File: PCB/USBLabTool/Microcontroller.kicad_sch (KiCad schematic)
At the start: 14 parts, among them U12 STM32H562VGTx, Y1 32.768kHz

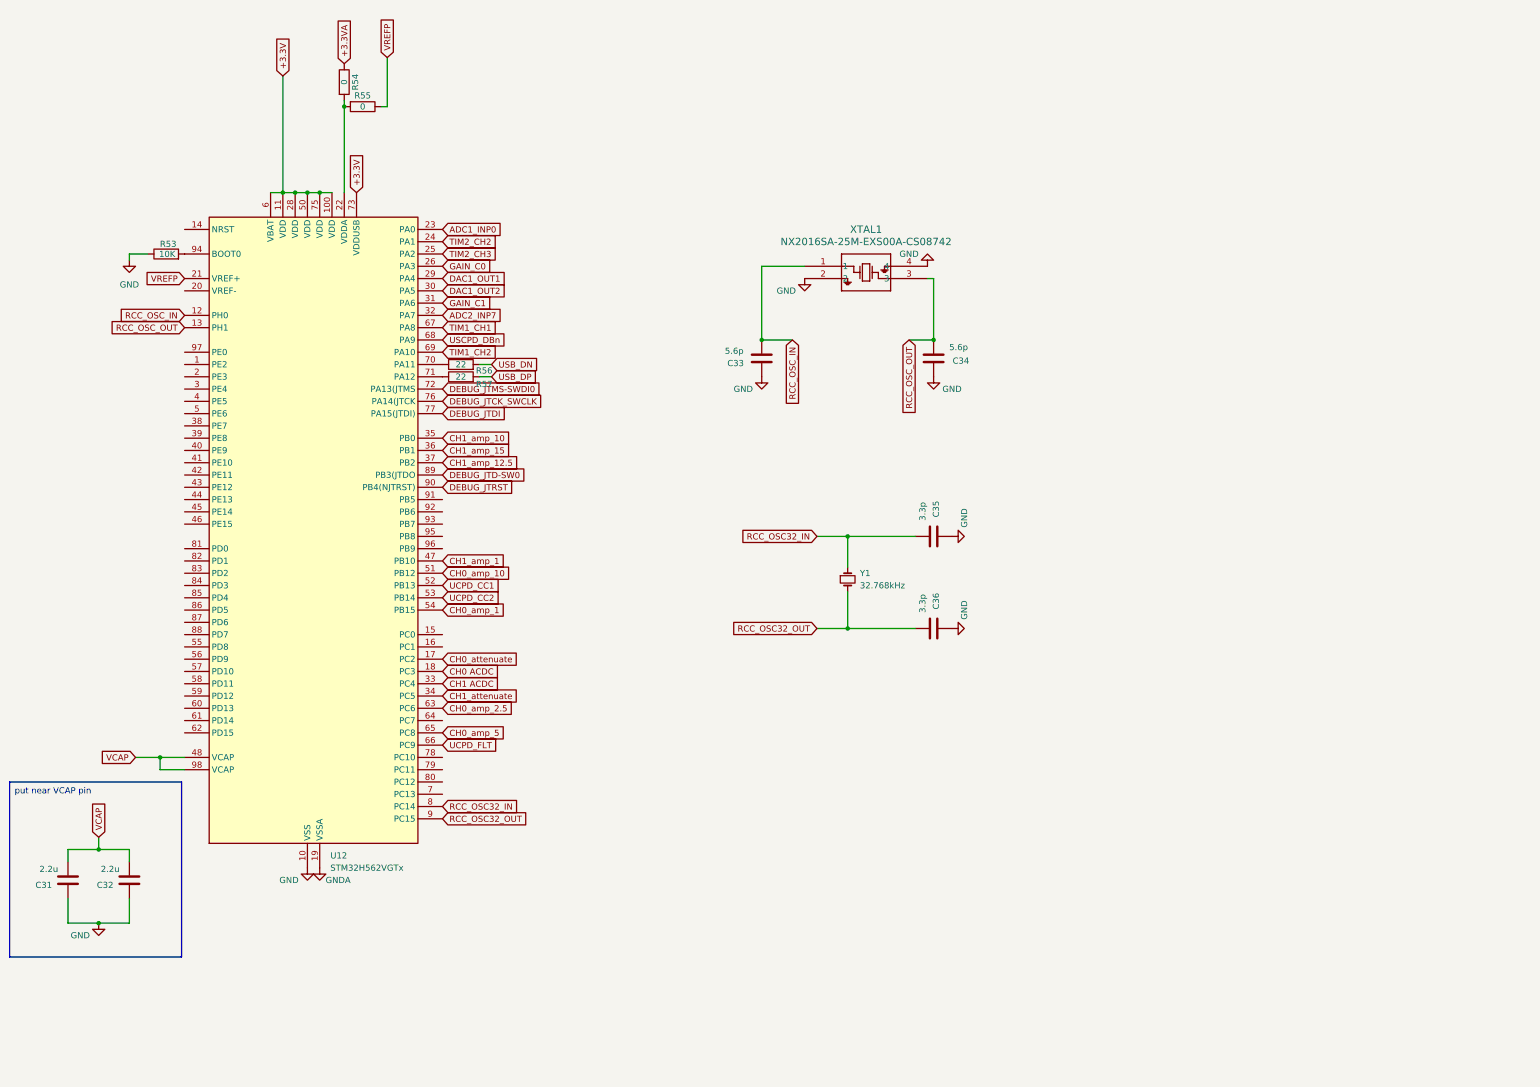
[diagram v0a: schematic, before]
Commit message: add NRST button and change MCU pins as latest
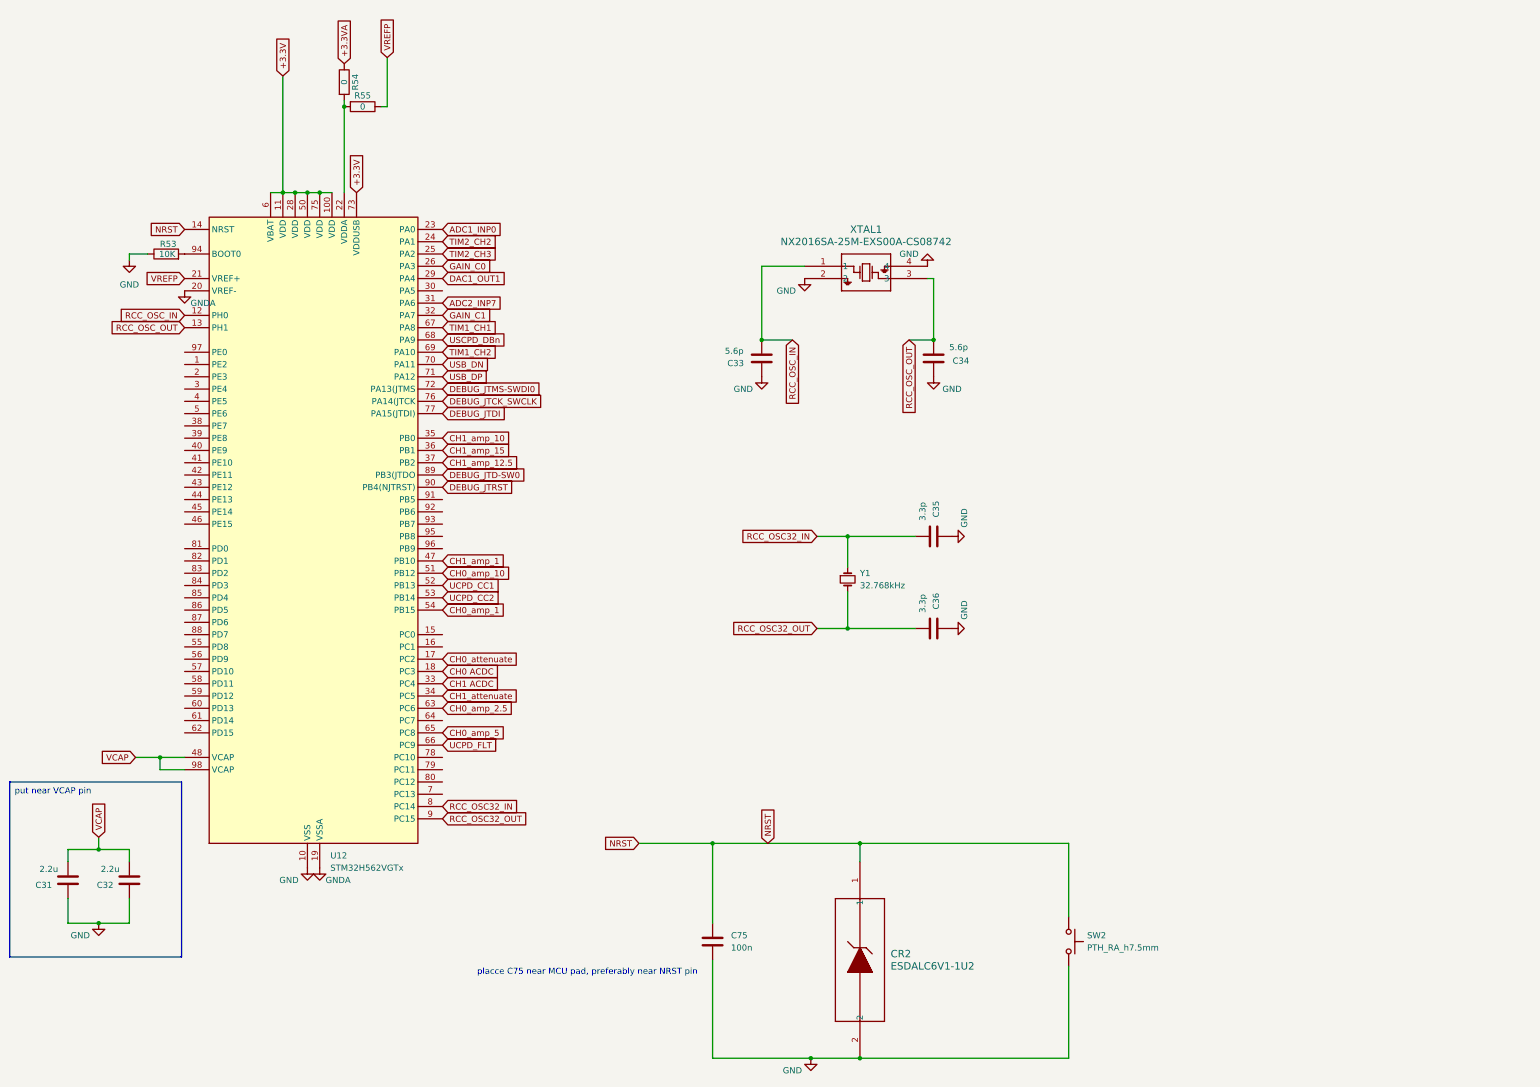
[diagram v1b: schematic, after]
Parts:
- removed R56, R57: 22, Resistor_SMD:R_0603_1608Metric_Pad0.98x0.95mm_HandSolder, symbol Device:R
- added C75: 100n, Capacitor_SMD:C_0603_1608Metric_Pad1.08x0.95mm_HandSolder, symbol Device:C
- added CR2: ESDALC6V1-1U2, DIODE_ESDALC6V1-1U2_STM, symbol ESDALC6V1-1U2:ESDALC6V1-1U2
- added SW2: PTH_RA_h7.5mm, SparkFun-Switch:Push_PTH_RA_8-020_h7.5mm, symbol SparkFun-Switch:SPST_Push_PTH_RA_h7.5mm
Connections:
- net ADC2_INP7: now also U12.31 (PA6); no longer U12.32 (PA7)
- net GAIN_C1: now also U12.32 (PA7); no longer U12.31 (PA6)
- net GND: now also C75.2, CR2.2, SW2.2
- net GNDA: now also U12.20 (VREF-)
- net USB_DN: now also U12.70 (PA11)
- net USB_DP: now also U12.71 (PA12)
- net NRST: now reaches U12.14 (NRST)
- net NRST: now also C75.1, CR2.1, SW2.1
- net DAC1_OUT2: no longer names the net of U12.30 (PA5)
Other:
- note added: "placce C75 near MCU pad, preferably near NRST pin"

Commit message: Fixed up footprints
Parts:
- SW2: footprint SparkFun-Switch:Push_PTH_RA_8-020_h7.5mm -> Button_Switch_THT:SW_PUSH_6mm_H7.3mm
- XTAL1: footprint footprintsgit:NX2016SA_NDK -> userfp:NX2016SA_NDK
- Y1: footprint SparkFun-Clock:Crystal_SMD_3.2x1.5mm -> Crystal:Crystal_SMD_MicroCrystal_CC7V-T1A-2Pin_3.2x1.5mm_HandSoldering

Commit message: Started adding 20pin
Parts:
- added J21: Conn_01x20_Pin, Connector_PinHeader_2.54mm:PinHeader_1x20_P2.54mm_Vertical, symbol Connector:Conn_01x20_Pin
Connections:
- net GND: now also J21.18 (Pin_18)
- net GNDA: now also J21.17 (Pin_17)
- new net P_CH0_IN: J21.20 (Pin_20)
- new net P_CH1_IN: J21.19 (Pin_19)

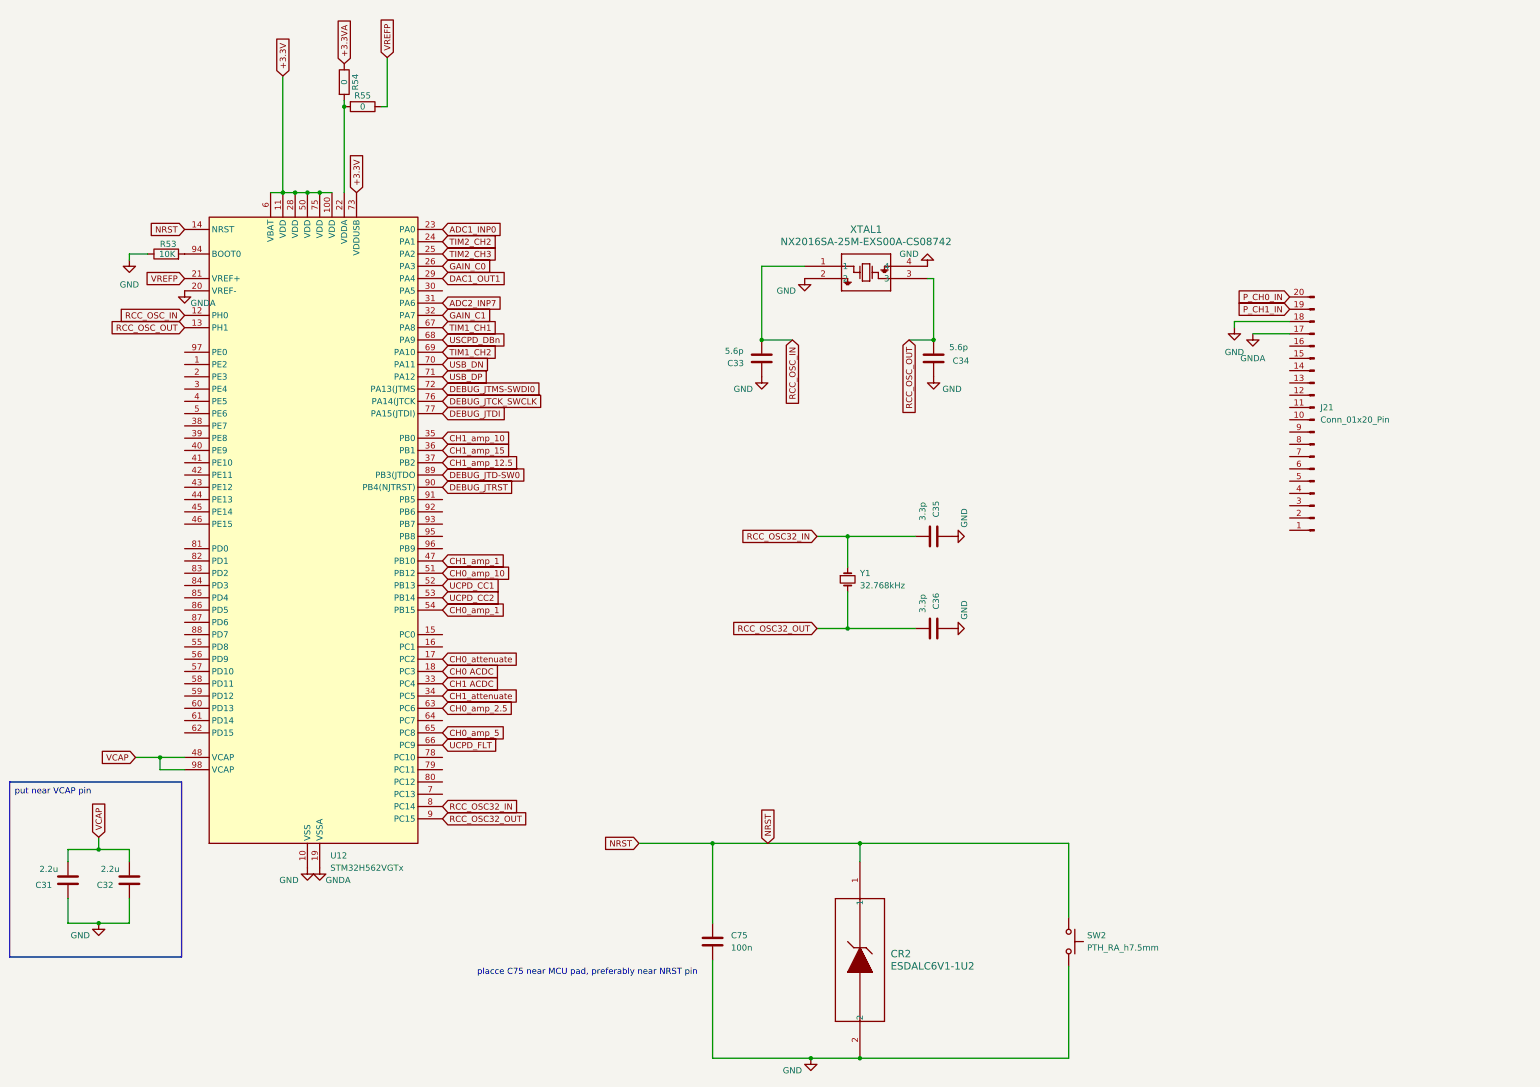
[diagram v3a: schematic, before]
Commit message: add Logic Analyzer and finish pins
Add Logic Analyzer. Add separate pins to 20 pins input(logic and scope) and 4 pins output(AWG). Add 4 programing pins.
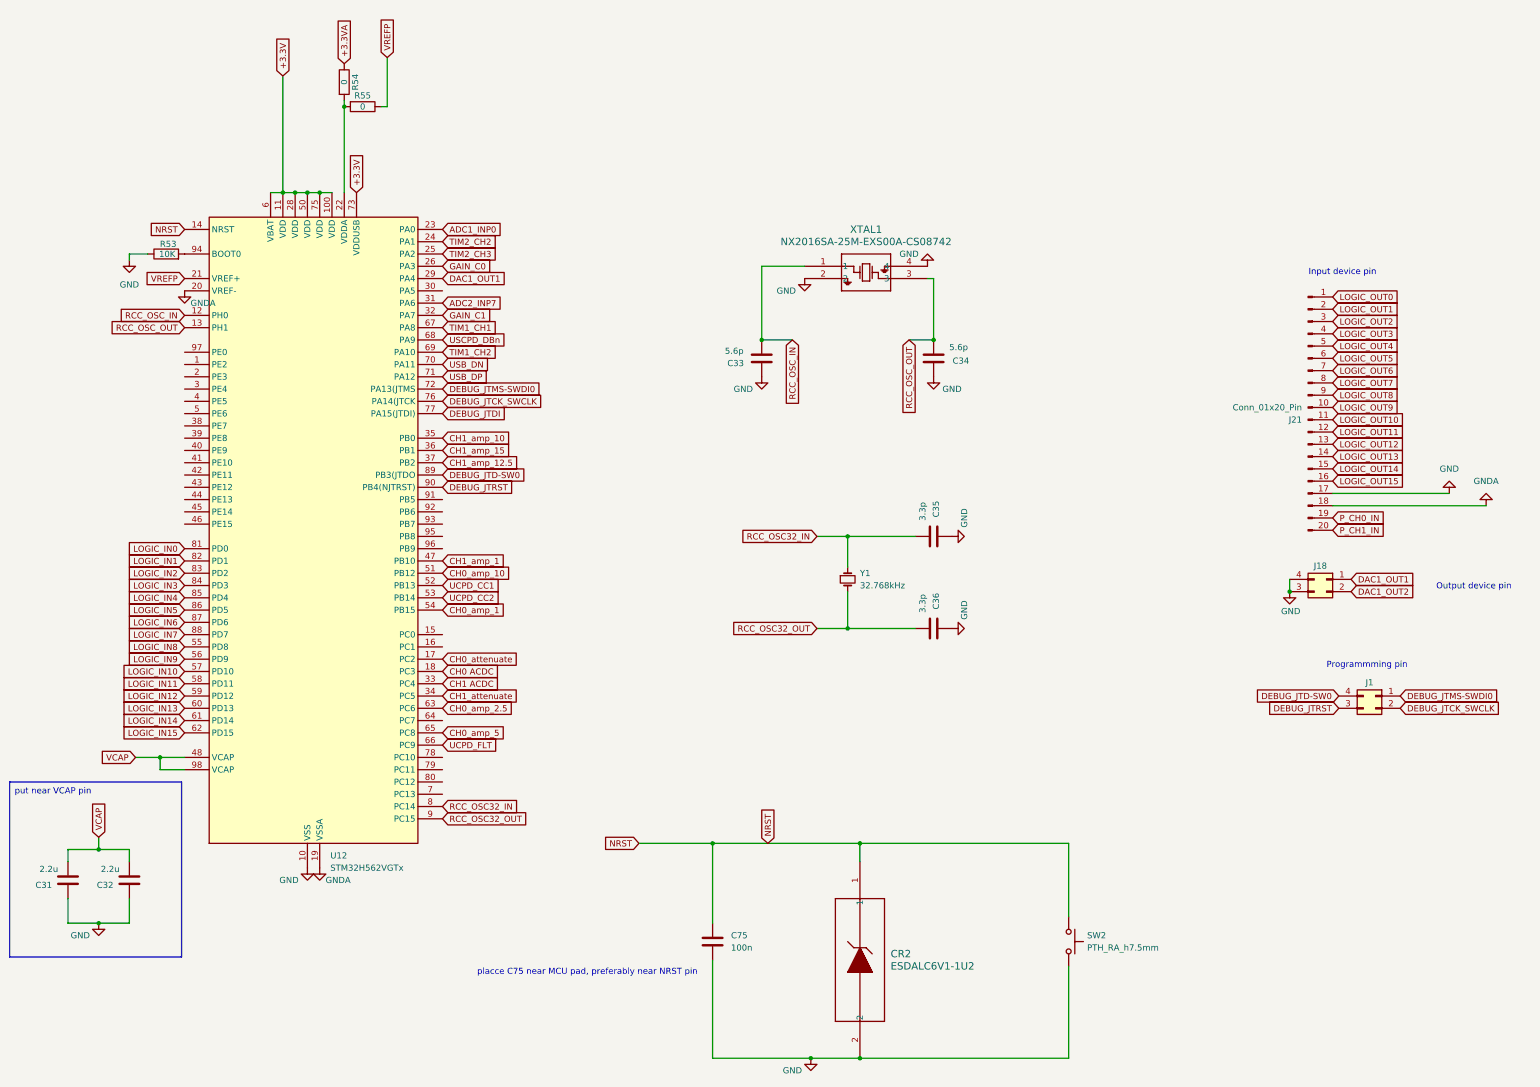
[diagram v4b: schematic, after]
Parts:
- added J1, J18: 02x02, awg_fp_lib:2x02, symbol Connector_Generic:Conn_02x02_Counter_Clockwise
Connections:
- net DAC1_OUT1: now also J18.1 (Pin_1)
- net DEBUG_JTCK_SWCLK: now also J1.2 (Pin_2)
- net DEBUG_JTD-SW0: now also J1.4 (Pin_4)
- net DEBUG_JTMS-SWDI0: now also J1.1 (Pin_1)
- net DEBUG_JTRST: now also J1.3 (Pin_3)
- net GND: now also J21.17 (Pin_17), J18.3 (Pin_3), J18.4 (Pin_4); no longer J21.18 (Pin_18)
- net GNDA: now also J21.18 (Pin_18); no longer J21.17 (Pin_17)
- net P_CH0_IN: now also J21.19 (Pin_19); no longer J21.20 (Pin_20)
- net P_CH1_IN: now also J21.20 (Pin_20); no longer J21.19 (Pin_19)
- net LOGIC_OUT0: now reaches J21.1 (Pin_1)
- net LOGIC_OUT9: now reaches J21.10 (Pin_10)
- net LOGIC_OUT10: now reaches J21.11 (Pin_11)
- net LOGIC_OUT11: now reaches J21.12 (Pin_12)
- net LOGIC_OUT12: now reaches J21.13 (Pin_13)
- net LOGIC_OUT13: now reaches J21.14 (Pin_14)
- net LOGIC_OUT14: now reaches J21.15 (Pin_15)
- net LOGIC_OUT15: now reaches J21.16 (Pin_16)
- net LOGIC_OUT1: now reaches J21.2 (Pin_2)
- net LOGIC_OUT2: now reaches J21.3 (Pin_3)
- net LOGIC_OUT3: now reaches J21.4 (Pin_4)
- net LOGIC_OUT4: now reaches J21.5 (Pin_5)
- net LOGIC_OUT5: now reaches J21.6 (Pin_6)
- net LOGIC_OUT6: now reaches J21.7 (Pin_7)
- net LOGIC_OUT7: now reaches J21.8 (Pin_8)
- net LOGIC_OUT8: now reaches J21.9 (Pin_9)
- net LOGIC_IN8: now reaches U12.55 (PD8)
- net LOGIC_IN9: now reaches U12.56 (PD9)
- net LOGIC_IN10: now reaches U12.57 (PD10)
- net LOGIC_IN11: now reaches U12.58 (PD11)
- net LOGIC_IN12: now reaches U12.59 (PD12)
- net LOGIC_IN13: now reaches U12.60 (PD13)
- net LOGIC_IN14: now reaches U12.61 (PD14)
- net LOGIC_IN15: now reaches U12.62 (PD15)
- net LOGIC_IN0: now reaches U12.81 (PD0)
- net LOGIC_IN1: now reaches U12.82 (PD1)
- net LOGIC_IN2: now reaches U12.83 (PD2)
- net LOGIC_IN3: now reaches U12.84 (PD3)
- net LOGIC_IN4: now reaches U12.85 (PD4)
- net LOGIC_IN5: now reaches U12.86 (PD5)
- net LOGIC_IN6: now reaches U12.87 (PD6)
- net LOGIC_IN7: now reaches U12.88 (PD7)
- new net DAC1_OUT2: J18.2 (Pin_2)
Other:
- note added: "Input device pin"
- note added: "Output device pin"
- note added: "Programmming pin"
- moved on the sheet: J21

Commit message: minor fixes
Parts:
- removed J1: 02x02, awg_fp_lib:2x02, symbol Connector_Generic:Conn_02x02_Counter_Clockwise
- added J1: Conn_01x06_Pin, Connector_PinHeader_2.54mm:PinHeader_1x06_P2.54mm_Vertical, symbol Connector:Conn_01x06_Pin
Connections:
- net +3.3V: now also J1.1 (Pin_1)
- net DAC1_OUT2: now also U12.30 (PA5)
- net DEBUG_JTCK_SWCLK: now also J1.2 (Pin_2)
- net DEBUG_JTD-SW0: now also J1.6 (Pin_6)
- net DEBUG_JTMS-SWDI0: now also J1.4 (Pin_4)
- net GND: now also SW2.M2, J1.3 (Pin_3)
- net NRST: now also SW2.M1, J1.5 (Pin_5)
- net CH1_amp_12.5 renamed CH1_amp_2.5
- net CH1_amp_15 renamed CH1_amp_5
- net LOGIC_OUT0 renamed LOGIC_INP0
- net LOGIC_OUT1 renamed LOGIC_INP1
- net LOGIC_OUT10 renamed LOGIC_INP10
- net LOGIC_OUT11 renamed LOGIC_INP11
- net LOGIC_OUT12 renamed LOGIC_INP12
- net LOGIC_OUT13 renamed LOGIC_INP13
- net LOGIC_OUT14 renamed LOGIC_INP14
- net LOGIC_OUT15 renamed LOGIC_INP15
- net LOGIC_OUT2 renamed LOGIC_INP2
- net LOGIC_OUT3 renamed LOGIC_INP3
- net LOGIC_OUT4 renamed LOGIC_INP4
- net LOGIC_OUT5 renamed LOGIC_INP5
- net LOGIC_OUT6 renamed LOGIC_INP6
- net LOGIC_OUT7 renamed LOGIC_INP7
- net LOGIC_OUT8 renamed LOGIC_INP8
- net LOGIC_OUT9 renamed LOGIC_INP9
- no-connect marks 0 -> 27
